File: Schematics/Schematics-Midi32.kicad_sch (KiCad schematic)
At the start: 1 part, among them J1 AudioJack2

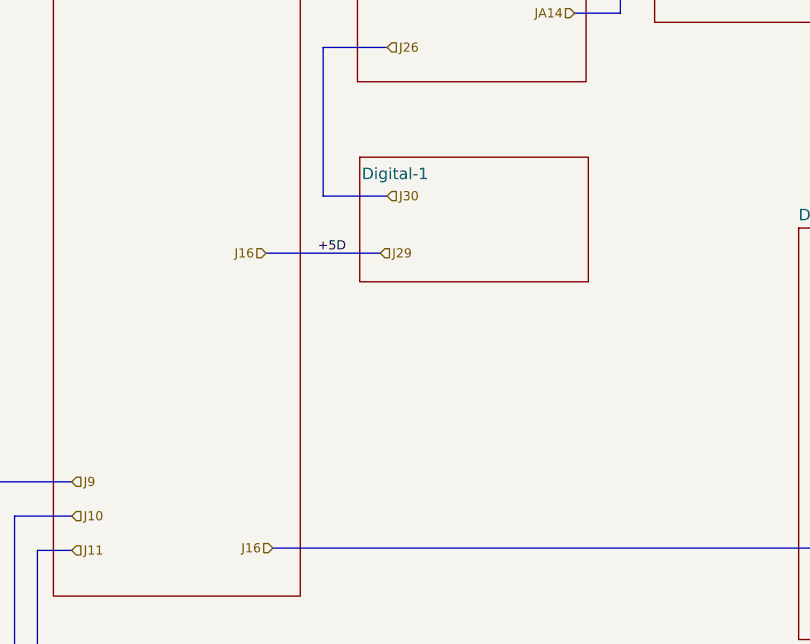
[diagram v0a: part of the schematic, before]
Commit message: Now with dual ESP32 with Midi32 and Disp32.
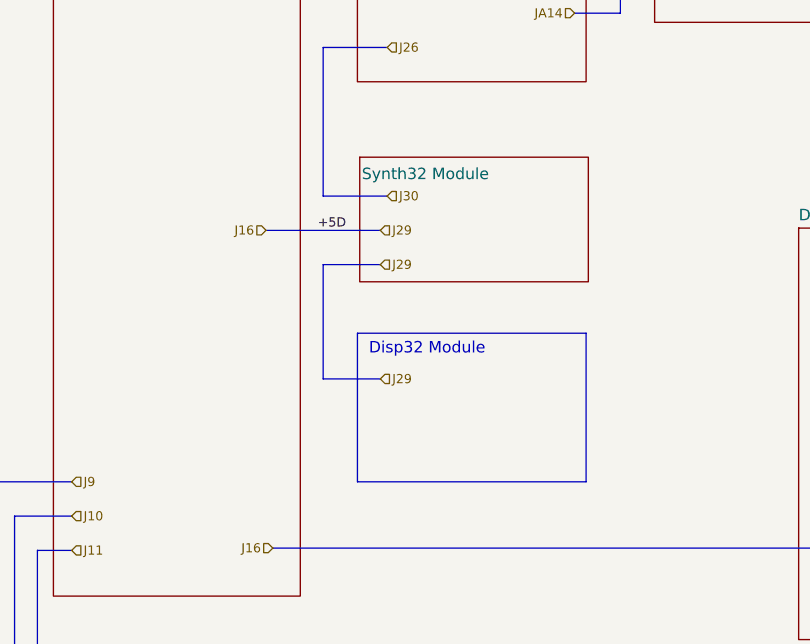
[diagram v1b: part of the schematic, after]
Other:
- sheet Digital-1 renamed Synth32 Module
- note added: "Disp32 Module"

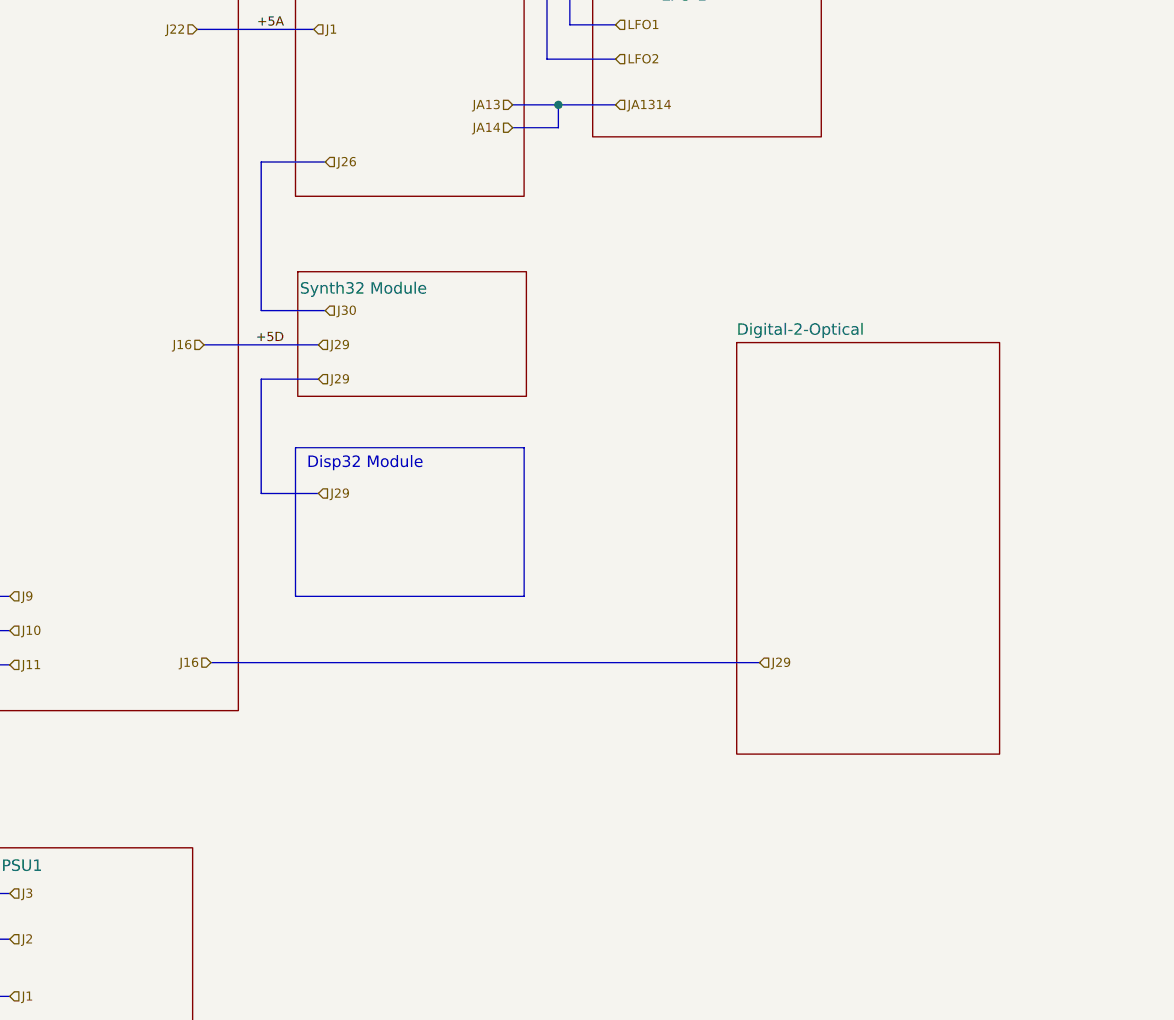
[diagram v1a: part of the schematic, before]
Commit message: Disp32 interface working properly.
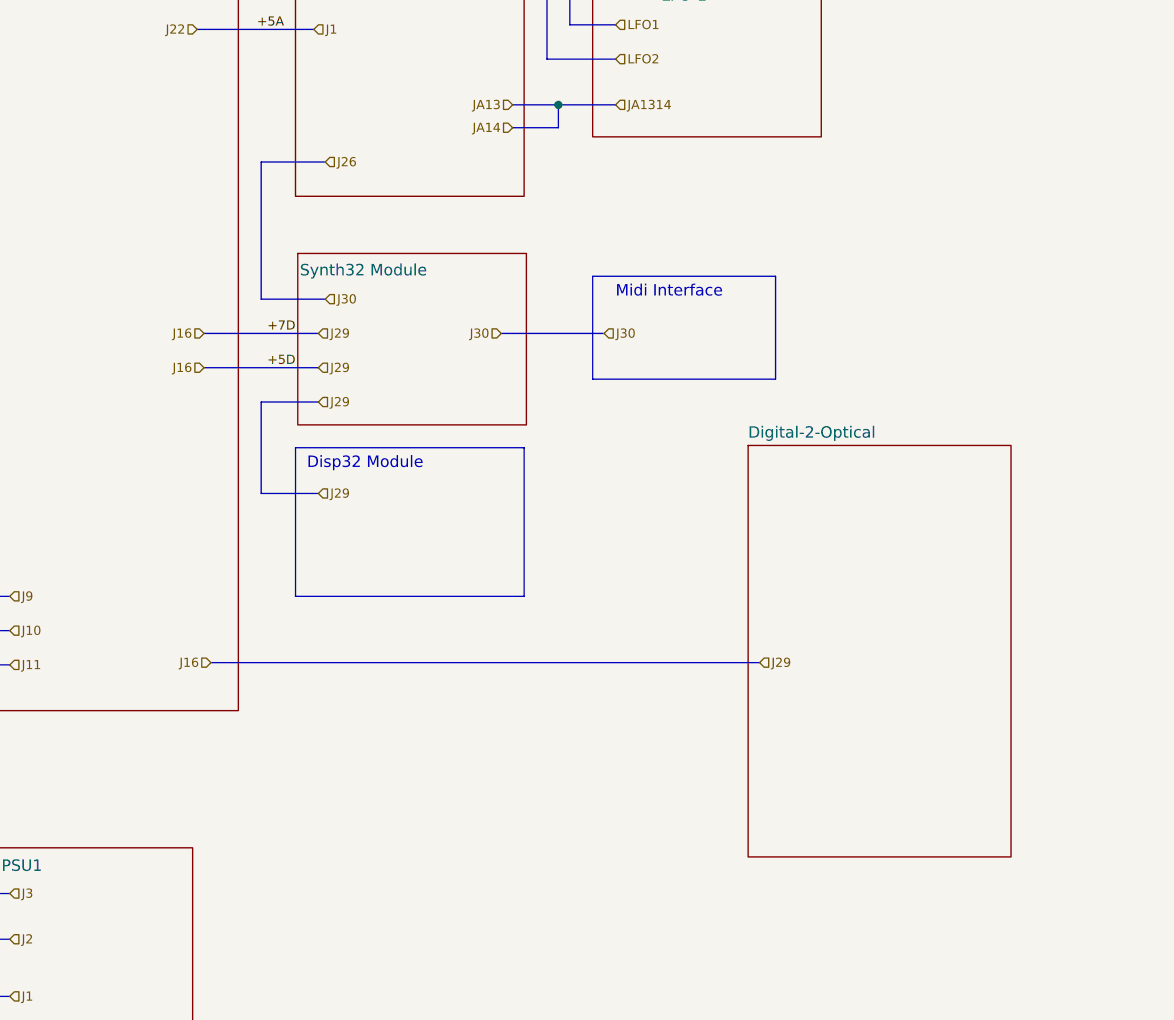
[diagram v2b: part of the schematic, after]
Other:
- note added: "Midi Interface"
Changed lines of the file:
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@@
   (junction (at 83.82 57.15) (diameter 0) (color 0 0 0 0)
   )
+  (bus (pts (xy 44.45 111.76) (xy 57.15 111.76))
+    (stroke (width 0) (type default))
+  )
   (bus (pts (xy 82.55 62.23) (xy 82.55 81.28))
     (stroke (width 0) (type default))
   )
-  (bus (pts (xy 57.15 116.84) (xy 50.8 116.84))
+  (bus (pts (xy 57.15 119.38) (xy 50.8 119.38))
     (stroke (width 0) (type default))
   )
@@
     (stroke (width 0) (type default))
   )
-  (bus (pts (xy 50.8 109.22) (xy 50.8 92.71))
+  (bus (pts (xy 50.8 107.95) (xy 50.8 92.71))
     (stroke (width 0) (type default))
   )
@@
     (stroke (width 0) (type default))
   )
+  (bus (pts (xy 77.47 111.76) (xy 88.9 111.76))
+    (stroke (width 0) (type default))
+  )
   (bus (pts (xy 163.83 25.4) (xy 175.26 25.4))
     (stroke (width 0) (type default))
@@
     (stroke (width 0) (type default))
   )
-  (bus (pts (xy 57.912 109.22) (xy 50.8 109.22))
+  (bus (pts (xy 57.912 107.95) (xy 50.8 107.95))
     (stroke (width 0) (type default))
   )
@@
     (stroke (width 0) (type default))
   )
-  (bus (pts (xy 50.8 116.84) (xy 50.8 129.54))
+  (bus (pts (xy 50.8 119.38) (xy 50.8 129.54))
     (stroke (width 0) (type default))
   )
@@
     (stroke (width 0) (type default))
   )
-  (bus (pts (xy 44.45 113.03) (xy 57.15 113.03))
+  (bus (pts (xy 44.45 115.57) (xy 57.15 115.57))
     (stroke (width 0) (type default))
   )
@@
     (stroke (width 0) (type default))
     (fill (type none))
+  )
+  (rectangle (start 87.63 105.41) (end 107.95 116.84)
+    (stroke (width 0) (type default))
+    (fill (type none))
+  )
+  (text "Midi Interface" (at 90.17 107.95 0)
+    (effects (font (size 1.27 1.27)) (justify left bottom))
   )
   (text "Disp32 Module" (at 55.88 127 0)
@@
     (effects (font (size 1.016 1.016)) (justify right bottom))
   )
-  (label "+5D" (at 53.34 113.03 180) (fields_autoplaced)
+  (label "+5D" (at 54.61 115.57 180) (fields_autoplaced)
     (effects (font (size 1.016 1.016)) (justify right bottom))
   )
@@
     (effects (font (size 0.762 0.762)) (justify left bottom))
   )
+  (label "+7D" (at 54.61 111.76 180) (fields_autoplaced)
+    (effects (font (size 1.016 1.016)) (justify right bottom))
+  )
   (label "±12A" (at 83.82 16.51 180) (fields_autoplaced)
     (effects (font (size 1.016 1.016)) (justify right bottom))
@@
     (effects (font (size 1.016 1.016)) (justify left))
   )
-  (hierarchical_label "J29" (shape input) (at 57.15 116.84 0) (fields_autoplaced)
+  (hierarchical_label "J29" (shape input) (at 57.15 119.38 0) (fields_autoplaced)
     (effects (font (size 1.016 1.016)) (justify left))
   )
@@
     (effects (font (size 1.016 1.016)) (justify right))
   )
-  (hierarchical_label "J16" (shape input) (at 44.45 113.03 180) (fields_autoplaced)
+  (hierarchical_label "J16" (shape input) (at 44.45 115.57 180) (fields_autoplaced)
     (effects (font (size 1.016 1.016)) (justify right))
   )
@@
     (effects (font (size 1.016 1.016)) (justify right))
   )
+  (hierarchical_label "J30" (shape input) (at 88.9 111.76 0) (fields_autoplaced)
+    (effects (font (size 1.016 1.016)) (justify left))
+  )
   (hierarchical_label "JA14" (shape input) (at 78.74 88.9 180) (fields_autoplaced)
     (effects (font (size 1.016 1.016)) (justify right))
@@
     (effects (font (size 1.016 1.016)) (justify right))
   )
+  (hierarchical_label "J16" (shape input) (at 44.45 111.76 180) (fields_autoplaced)
+    (effects (font (size 1.016 1.016)) (justify right))
+  )
   (hierarchical_label "JA78" (shape input) (at 90.17 46.99 0) (fields_autoplaced)
     (effects (font (size 1.016 1.016)) (justify left))
@@
     (effects (font (size 1.016 1.016)) (justify left))
   )
+  (hierarchical_label "J30" (shape input) (at 77.47 111.76 180) (fields_autoplaced)
+    (effects (font (size 1.016 1.016)) (justify right))
+  )
   (hierarchical_label "JA12" (shape input) (at 78.74 59.69 180) (fields_autoplaced)
     (effects (font (size 1.016 1.016)) (justify right))
@@
     (effects (font (size 1.016 1.016)) (justify right))
   )
-  (hierarchical_label "J30" (shape input) (at 57.912 109.22 0) (fields_autoplaced)
+  (hierarchical_label "J30" (shape input) (at 57.912 107.95 0) (fields_autoplaced)
     (effects (font (size 1.016 1.016)) (justify left))
   )
@@
     (effects (font (size 1.016 1.016)) (justify left))
   )
-  (hierarchical_label "J29" (shape input) (at 57.15 113.03 0) (fields_autoplaced)
+  (hierarchical_label "J29" (shape input) (at 57.15 115.57 0) (fields_autoplaced)
+    (effects (font (size 1.016 1.016)) (justify left))
+  )
+  (hierarchical_label "J29" (shape input) (at 57.15 111.76 0) (fields_autoplaced)
     (effects (font (size 1.016 1.016)) (justify left))
   )
@@
     )
   )
-  (sheet (at 103.632 112.776) (size 29.21 45.72) (fields_autoplaced)
+  (sheet (at 104.902 124.206) (size 29.21 45.72) (fields_autoplaced)
     (stroke (width 0.1524) (type solid))
     (fill (color 0 0 0 0.0000))
-    (property "Sheetname" "Digital-2-Optical" (at 103.632 112.0644 0)
+    (property "Sheetname" "Digital-2-Optical" (at 104.902 123.4944 0)
       (effects (font (size 1.27 1.27)) (justify left bottom))
     )
-    (property "Sheetfile" "DigitalOptical.kicad_sch" (at 103.632 159.0806 0)
+    (property "Sheetfile" "DigitalOptical.kicad_sch" (at 104.902 170.5106 0)
       (effects (font (size 1.27 1.27)) (justify left top) hide)
     )
@@
     )
   )
-  (sheet (at 54.864 104.902) (size 25.4 13.843)
+  (sheet (at 54.864 102.87) (size 25.4 19.05)
     (stroke (width 0.1524) (type solid))
     (fill (color 0 0 0 0.0000))
-    (property "Sheetname" "Synth32 Module" (at 55.0926 107.4928 0)
+    (property "Sheetname" "Synth32 Module" (at 55.0926 105.4608 0)
       (effects (font (size 1.27 1.27)) (justify left bottom))
     )
-    (property "Sheetfile" "Digitial-1.kicad_sch" (at 54.7878 116.4082 0)
+    (property "Sheetfile" "Digitial-1.kicad_sch" (at 54.7878 114.3762 0)
       (effects (font (size 1.016 1.016)) (justify left top) hide)
     )
